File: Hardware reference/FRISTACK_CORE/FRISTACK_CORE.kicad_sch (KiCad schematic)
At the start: 72 parts, among them J1 USB_C_Receptacle_USB2.0_16P, J3 Conn_01x04_Pin, J4 Conn_01x09_Socket, J5 Conn_01x12_Socket, J6 Conn_01x12_Socket, J7 Conn_01x04_Pin, J8 Conn_01x02_Pin, U1 AZ1117-3.3, U2 USBLC6-2SC6, U3 ESP32-S3-MINI-1U, U4 SN65HVD232, Y1 32.768 kHz

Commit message: Updated CORE schematic and PCB design
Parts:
- removed J5, J6: Conn_01x12_Socket, Connector_PinSocket_2.54mm:PinSocket_1x12_P2.54mm_Vertical, symbol Connector:Conn_01x12_Socket
- added J5, J6: Conn_01x13_Socket, Connector_PinSocket_2.54mm:PinSocket_1x13_P2.54mm_Vertical, symbol Connector:Conn_01x13_Socket
- added J8: Conn_01x02_Pin, Connector_PinHeader_2.54mm:PinHeader_1x02_P2.54mm_Vertical, symbol Connector:Conn_01x02_Pin
- added R22: 120, Resistor_SMD:R_0603_1608Metric, symbol Device:R
- renumbered J8 to J2, R15 to R10, R16 to R11, R8 to R12, R9 to R13, R10 to R14, R11 to R15, R12 to R16, R13 to R17, R17 to R18, R18 to R19, R19 to R20, R20 to R21, R21 to R8, R14 to R9
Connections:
- net GPIO10 is gone; now on net CS: U3.14 (IO10)
- net GPIO11 is gone; now on net MISO: U3.15 (IO11)
- net GPIO12 is gone; now on net SCK: U3.16 (IO12)
- net +3V3: now also J5.13 (Pin_13)
- net +5V: now also J6.13 (Pin_13)
- net ADC_1: now also J5.2 (Pin_2)
- net CAN_D: now also U3.37 (IO41); no longer U3.18 (IO14)
- net CAN_H: now also J6.3 (Pin_3), R22.1
- net CAN_L: now also J6.2 (Pin_2), J8.2 (Pin_2)
- net CAN_R: now also U3.38 (IO42); no longer U3.17 (IO13)
- net CS: now also J6.7 (Pin_7); no longer U3.29 (IO34)
- net EN: now also J6.12 (Pin_12)
- net GND: now also J5.1 (Pin_1), J6.1 (Pin_1)
- net GPIO39: now also J6.8 (Pin_8)
- net I2S_DIN: now also J5.9 (Pin_9)
- net I2S_DOUT: now also J5.8 (Pin_8)
- net I2S_LRCK: now also J5.10 (Pin_10)
- net MISO: now also J6.6 (Pin_6); no longer U3.33 (IO37)
- net MOSI: now also U3.17 (IO13), J6.4 (Pin_4); no longer U3.31 (IO35)
- net SCK: now also J6.5 (Pin_5); no longer U3.32 (IO36)
- net SCL: now also J5.6 (Pin_6)
- net SDA: now also J5.7 (Pin_7)
- net UART0_RX: now also J6.10 (Pin_10)
- net UART0_TX: now also J6.11 (Pin_11)
- net USB_DN: now also U2.6 (I/O1); no longer U2.4 (I/O2)
- net USB_DN_2: now also U2.1 (I/O1), J5.11 (Pin_11); no longer U2.3 (I/O2)
- net USB_DP: now also U2.4 (I/O2); no longer U2.6 (I/O1)
- net USB_DP_2: now also U2.3 (I/O2), J5.12 (Pin_12); no longer U2.1 (I/O1)
- net GPIO17: now reaches U3.21 (IO17)
- net GPIO17: now also J5.4 (Pin_4)
- net GPIO18: now reaches U3.22 (IO18)
- net GPIO18: now also J5.3 (Pin_3)
- net GPIO40: now reaches U3.36 (IO40)
- net GPIO40: now also J6.9 (Pin_9)
- net GPIO38: no longer names the net of U3.34 (IO38)
- new net: J8.1 (Pin_1), R22.2
- new net GPIO14: J5.5 (Pin_5), U3.18 (IO14)
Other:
- note removed: "JST"
- moved on the sheet: C17, C18, C6, C7, C8, C9, D4, J7, R18, R19, S1, S2

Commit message: Added SENSOR-NODE and reworked CORE
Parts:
- removed C13: 22uF, Capacitor_SMD:C_0603_1608Metric, symbol Device:C
- removed C31: 2.2uF, Capacitor_SMD:C_0603_1608Metric, symbol Device:C
- removed C32: 100nF, Capacitor_SMD:C_0603_1608Metric, symbol Device:C
- removed C33: 1nF, Capacitor_SMD:C_0603_1608Metric, symbol Device:C
- removed D3: 1N5819WS, Diode_SMD:D_SOD-323, symbol Diode:1N5819WS
- removed J2: Conn_01x02_Pin, Connector_JST:JST_PH_S2B-PH-K_1x02_P2.00mm_Horizontal, symbol Connector:Conn_01x02_Pin
- removed J4: Conn_01x09_Socket, Connector_PinSocket_2.54mm:PinSocket_1x09_P2.54mm_Vertical, symbol Connector:Conn_01x09_Socket
- added D4: 1N5819WS, Diode_SMD:D_SOD-323, symbol Diode:1N5819WS
- added J3: Conn_01x02_Pin, Connector_PinHeader_2.54mm:PinHeader_1x02_P2.54mm_Vertical, symbol Connector:Conn_01x02_Pin
- added PROG1: Conn_01x04_Pin, Connector_JST:JST_PH_S4B-PH-K_1x04_P2.00mm_Horizontal, symbol Connector:Conn_01x04_Pin
- added R17: 10K, Resistor_SMD:R_0603_1608Metric, symbol Device:R
- added U4: FUSB42, Package_SO:VSSOP-10_3x3mm_P0.5mm, symbol Interface_USB:TS3USB30EDGSR
- R10: renamed from R12; value 2K2 -> 4K7
- R11: renamed from R13; value 2K2 -> 4K7
- R16: renamed from R10; value 0 -> 22
- R7: value 499 -> 22
- R8, R9: value 0 -> 22
- renumbered S2 to Boot1, C6 to C2, C7 to C3, C8 to C4, C9 to C5, C2 to C6, C3 to C7, C4 to C8, C5 to C9, D4 to D5, J5 to J4, J6 to J5, J8 to J6, R14 to R12, R15 to R13, R16 to R14, R17 to R15, R11 to R18, R22 to R19, R18 to R20, R19 to R21, R20 to R22, R21 to R23, S1 to RST1, J7 to TWAI1, U4 to U5, J3 to UART1
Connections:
- net +3V3: now also UART1.4 (Pin_4), PROG1.1 (Pin_1), R17.1, U4.10 (VCC); no longer UART1.3 (Pin_3)
- net ADC_1: now also J4.5 (Pin_5); no longer J4.2 (Pin_2)
- net GND: now also UART1.3 (Pin_3), PROG1.2 (Pin_2), U4.5 (GND), U4.9 (~{OE}); no longer UART1.4 (Pin_4)
- net GPIO14: now also J4.4 (Pin_4); no longer J4.5 (Pin_5)
- net GPIO17: now also J4.3 (Pin_3); no longer J4.4 (Pin_4)
- net GPIO18: now also J4.2 (Pin_2); no longer J4.3 (Pin_3)
- net DC: no longer names the net of U3.30 (IO48)
- net RST_LCD renamed GPIO47
- net GPIO47: now also D4.2 (A)
- net USB_DN renamed USB_N
- removed net USB_DN_2: J4.11 (Pin_11), R9.2, U2.1 (I/O1)
- net USB_DP renamed USB_P
- removed net USB_DP_2: J4.12 (Pin_12), R16.2, U2.3 (I/O2)
- new net: D4.1 (K), J3.2 (Pin_2), U4.1 (S)
- new net: J3.1 (Pin_1), R17.2
- new net USB_N_2: U2.1 (I/O1), U4.7 (D2-)
- new net USB_N_ESP: R9.2, U4.6 (D-)
- new net USB_N_HD: J4.12 (Pin_12), PROG1.3 (Pin_3), U4.2 (D1+)
- new net USB_P_2: U2.3 (I/O2), U4.3 (D2+)
- new net USB_P_ESP: R16.2, U4.4 (D+)
- new net USB_P_HD: J4.11 (Pin_11), PROG1.4 (Pin_4), U4.8 (D1-)
- no-connect marks 15 -> 16
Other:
- note removed: "Setup for ILI9341"
- moved on the sheet: C15, C16, R10, R11, R12, R13, R14, R15, R18, UART1, Y1

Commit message: Power management changes on CORE and SENSOR_NODE
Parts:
- removed Boot1, RST1: TL3315NF100Q, User_imports:SW_TL3315NF100Q, symbol User_imports:TL3315NF100Q
- removed C8: 0.1uF, Capacitor_SMD:C_0603_1608Metric, symbol Device:C
- removed C9: 10uF, Capacitor_SMD:C_0603_1608Metric, symbol Device:C
- removed D2: LED RED, LED_SMD:LED_0805_2012Metric, symbol Device:LED
- removed D4: 1N5819WS, Diode_SMD:D_SOD-323, symbol Diode:1N5819WS
- removed J3: Conn_01x02_Pin, Connector_PinHeader_2.54mm:PinHeader_1x02_P2.54mm_Vertical, symbol Connector:Conn_01x02_Pin
- removed R17: 10K, Resistor_SMD:R_0603_1608Metric, symbol Device:R
- removed U1: AZ1117-3.3, Package_TO_SOT_SMD:SOT-223, symbol Regulator_Linear:AZ1117-3.3
- removed U4: FUSB42, Package_SO:VSSOP-10_3x3mm_P0.5mm, symbol Interface_USB:TS3USB30EDGSR
- added L1: 2.2uH, Inductor_SMD:L_0805_2012Metric, symbol Device:L
- added S1, S2: TS-1088-AR02016, User_imports:SW_TS-1088-AR02016, symbol TS-1088-AR02016:TS-1088-AR02016
- added U1: TPS62840DLCR, User_imports:SON50P200X150X100-8N, symbol TPS62840DLCR:TPS62840DLCR
- C6: value 10uF -> 4.7uF
- C7: value 0.1uF -> 10uF
- R3: value 75 -> 267k
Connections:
- net USB_N_ESP is gone; now on net USB_N_2: R9.2
- net USB_N_HD is gone; now on net USB_N_2: J4.12 (Pin_12), PROG1.3 (Pin_3)
- net USB_P_ESP is gone; now on net USB_P_2: R16.2
- net USB_P_HD is gone; now on net USB_P_2: J4.11 (Pin_11), PROG1.4 (Pin_4)
- net +3V3: now also C7.1, L1.2, U1.8 (VOS); no longer R3.1
- net +5V: now also U1.2 (VIN), U1.4 (EN); no longer C7.1
- net EN: now also S1.2; no longer J5.12 (Pin_12)
- net GND: now also J5.8 (Pin_8), R3.2, S1.1, S2.1, U1.1 (GND), U1.3 (MODE), U1.6 (STOP)
- net GPIO0: now also S2.2
- net UART0_RX: now also J5.11 (Pin_11); no longer J5.10 (Pin_10)
- net UART0_TX: now also J5.12 (Pin_12); no longer J5.11 (Pin_11)
- net GPIO39 renamed RST
- net RST: now also J5.9 (Pin_9); no longer J5.8 (Pin_8)
- net GPIO40 renamed BOOT
- net BOOT: now also J5.10 (Pin_10); no longer J5.9 (Pin_9)
- net GPIO47: no longer names the net of U3.27 (IO47)
- new net: R3.1, U1.5 (VSET)
- new net: L1.1, U1.7 (SW)
- no-connect marks 16 -> 17
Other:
- moved on the sheet: C2, C3, C4, C5

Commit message: Added logos, annotations
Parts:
- added D2: 1N5819WS, Diode_SMD:D_SOD-323, symbol Diode:1N5819WS
- added J2: JTAG_PIN_HEADER, Connector_PinHeader_2.54mm:PinHeader_1x02_P2.54mm_Vertical, symbol Connector:Conn_01x02_Pin
- added J3: BAT, Connector_JST:JST_PH_S2B-PH-K_1x02_P2.00mm_Horizontal, symbol Connector:Conn_01x02_Pin
- C6, C7: footprint Capacitor_SMD:C_0603_1608Metric -> Capacitor_SMD:C_0402_1005Metric
- L1: footprint Inductor_SMD:L_0805_2012Metric -> User imports:INDC2016X120N
- R18: value ? -> 1M
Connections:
- net +3V3: now also TWAI1.4 (Pin_4); no longer TWAI1.3 (Pin_3)
- net +5V: now also D2.2 (A)
- net CAN_D: now also J2.2 (Pin_2)
- net CAN_R: now also J2.1 (Pin_1)
- net GND: now also TWAI1.3 (Pin_3), J3.2 (Pin_2); no longer TWAI1.4 (Pin_4)
- new net: D2.1 (K), J3.1 (Pin_1)

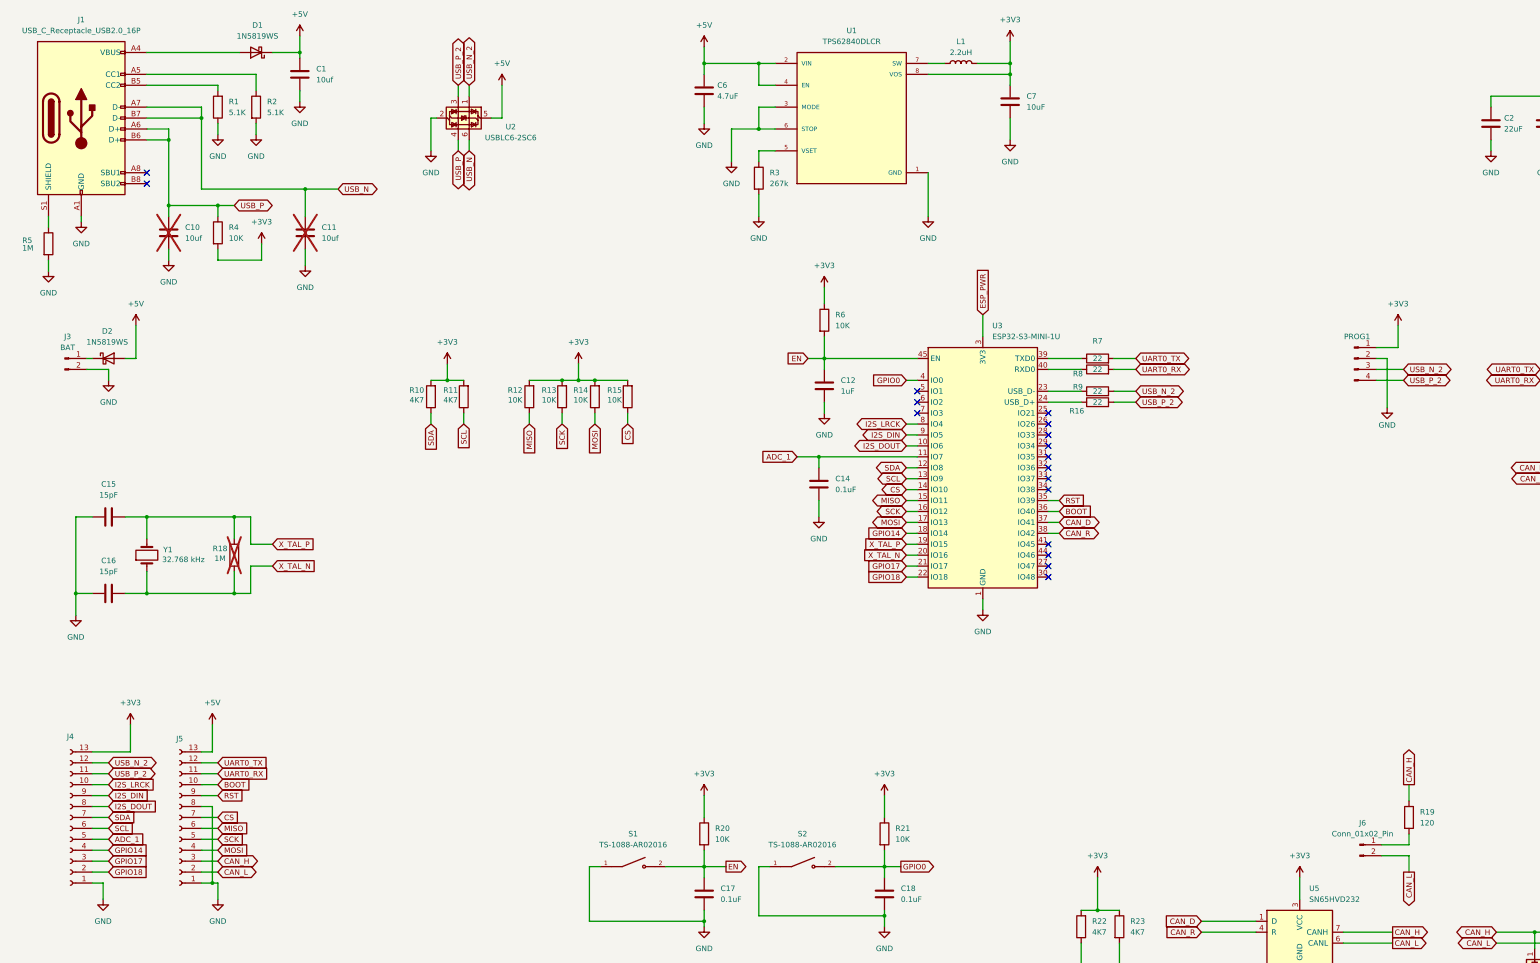
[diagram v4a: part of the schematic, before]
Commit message: Added USBSwitch to Core and added first version of Compatibility
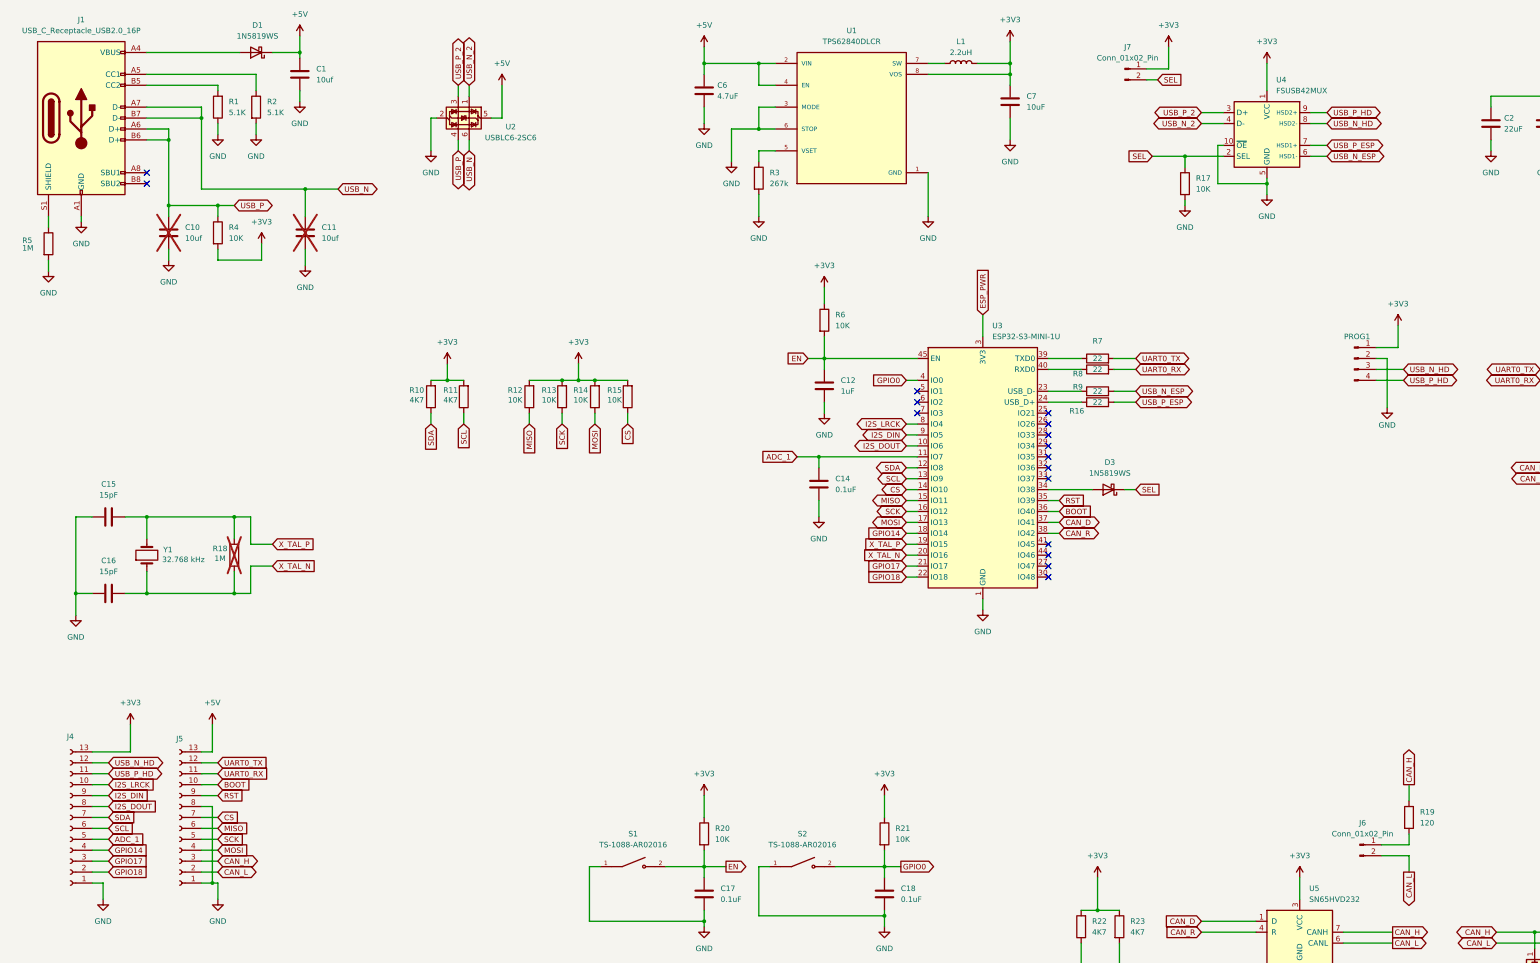
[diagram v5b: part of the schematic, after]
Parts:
- removed D2: 1N5819WS, Diode_SMD:D_SOD-323, symbol Diode:1N5819WS
- removed J3: BAT, Connector_JST:JST_PH_S2B-PH-K_1x02_P2.00mm_Horizontal, symbol Connector:Conn_01x02_Pin
- added D3: 1N5819WS, Diode_SMD:D_SOD-323, symbol Diode:1N5819WS
- added J7: Conn_01x02_Pin, Connector_PinHeader_2.54mm:PinHeader_1x02_P2.54mm_Vertical, symbol Connector:Conn_01x02_Pin
- added R17: 10K, Resistor_SMD:R_0603_1608Metric, symbol Device:R
- added U4: FSUSB42MUX, Package_SO:MSOP-10_3x3mm_P0.5mm, symbol Interface_USB:FSUSB42MUX
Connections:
- net +3V3: now also J7.1 (Pin_1), U4.1 (VCC)
- net GND: now also R17.2, U4.10 (~{OE}), U4.5 (GND)
- net USB_N_2: now also U4.4 (D-); no longer J4.12 (Pin_12), PROG1.3 (Pin_3), R9.2
- net USB_P_2: now also U4.3 (D+); no longer J4.11 (Pin_11), PROG1.4 (Pin_4), R16.2
- net at U3.34 (IO38): now also D3.2 (A)
- new net SEL: D3.1 (K), J7.2 (Pin_2), R17.1, U4.2 (SEL)
- new net USB_N_ESP: R9.2, U4.6 (HSD1-)
- new net USB_N_HD: J4.12 (Pin_12), PROG1.3 (Pin_3), U4.8 (HSD2-)
- new net USB_P_ESP: R16.2, U4.7 (HSD1+)
- new net USB_P_HD: J4.11 (Pin_11), PROG1.4 (Pin_4), U4.9 (HSD2+)
- no-connect marks 17 -> 16

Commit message: Reworked CORE and adjusted header pins
Added USB switch and MCP73871 for charging battery and powering the system. Changed GPIO14 to BAT, dedicated for battery.
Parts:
- added C15: 10uf, Capacitor_SMD:C_0402_1005Metric, symbol Device:C
- added C21, C22: 4.7uF, Capacitor_SMD:C_0402_1005Metric, symbol Device:C
- added R12: 20k, Resistor_SMD:R_0402_1005Metric, symbol Device:R
- added R13: 330k, Resistor_SMD:R_0402_1005Metric, symbol Device:R
- added R14: 110k, Resistor_SMD:R_0402_1005Metric, symbol Device:R
- added R15: 2k, Resistor_SMD:R_0402_1005Metric, symbol Device:R
- added R16, R17, R18, R20, R22, R23: 10k, Resistor_SMD:R_0402_1005Metric, symbol Device:R
- added TH1: 10k, Resistor_SMD:R_0603_1608Metric, symbol Device:Thermistor_NTC
- added U2: MCP73871-2CC, Package_DFN_QFN:QFN-20-1EP_4x4mm_P0.5mm_EP2.5x2.5mm, symbol Battery_Management:MCP73871-2CC
- C1: renamed from C19; footprint Capacitor_SMD:C_0603_1608Metric -> Capacitor_SMD:C_0402_1005Metric
- C10: renamed from C11; footprint Capacitor_SMD:C_0603_1608Metric -> Capacitor_SMD:C_0402_1005Metric
- C11: renamed from C24; footprint Capacitor_SMD:C_0603_1608Metric -> Capacitor_SMD:C_0402_1005Metric
- C12: renamed from C25; footprint Capacitor_SMD:C_0603_1608Metric -> Capacitor_SMD:C_0402_1005Metric
- C13: renamed from C26; footprint Capacitor_SMD:C_0603_1608Metric -> Capacitor_SMD:C_0402_1005Metric
- C14: renamed from C27; footprint Capacitor_SMD:C_0603_1608Metric -> Capacitor_SMD:C_0402_1005Metric
- C16: renamed from C28; footprint Capacitor_SMD:C_0603_1608Metric -> Capacitor_SMD:C_0402_1005Metric
- C17: renamed from C29; footprint Capacitor_SMD:C_0603_1608Metric -> Capacitor_SMD:C_0402_1005Metric
- C19: renamed from C30; footprint Capacitor_SMD:C_0603_1608Metric -> Capacitor_SMD:C_0402_1005Metric
- C2: renamed from C20; footprint Capacitor_SMD:C_0603_1608Metric -> Capacitor_SMD:C_0402_1005Metric
- C20: renamed from C17; footprint Capacitor_SMD:C_0603_1608Metric -> Capacitor_SMD:C_0402_1005Metric
- C23: renamed from C18; footprint Capacitor_SMD:C_0603_1608Metric -> Capacitor_SMD:C_0402_1005Metric
- C24: renamed from C14; footprint Capacitor_SMD:C_0603_1608Metric -> Capacitor_SMD:C_0402_1005Metric
- C25: renamed from C12; footprint Capacitor_SMD:C_0603_1608Metric -> Capacitor_SMD:C_0402_1005Metric
- C27: renamed from C2; footprint Capacitor_SMD:C_0603_1608Metric -> Capacitor_SMD:C_0402_1005Metric
- C28: renamed from C3; footprint Capacitor_SMD:C_0603_1608Metric -> Capacitor_SMD:C_0402_1005Metric
- C29: renamed from C4; footprint Capacitor_SMD:C_0603_1608Metric -> Capacitor_SMD:C_0402_1005Metric
- C3: renamed from C15; footprint Capacitor_SMD:C_0603_1608Metric -> Capacitor_SMD:C_0402_1005Metric
- C30: renamed from C5; footprint Capacitor_SMD:C_0603_1608Metric -> Capacitor_SMD:C_0402_1005Metric
- C4: renamed from C16; footprint Capacitor_SMD:C_0603_1608Metric -> Capacitor_SMD:C_0402_1005Metric
- C5: renamed from C21; footprint Capacitor_SMD:C_0603_1608Metric -> Capacitor_SMD:C_0402_1005Metric
- C6: renamed from C10; footprint Capacitor_SMD:C_0603_1608Metric -> Capacitor_SMD:C_0402_1005Metric
- C7: renamed from C22; footprint Capacitor_SMD:C_0603_1608Metric -> Capacitor_SMD:C_0402_1005Metric
- C8: renamed from C23; footprint Capacitor_SMD:C_0603_1608Metric -> Capacitor_SMD:C_0402_1005Metric
- C9: renamed from C1; footprint Capacitor_SMD:C_0603_1608Metric -> Capacitor_SMD:C_0402_1005Metric
- L1: footprint User imports:INDC2016X120N -> User_imports:INDC2016X120N
- R1: renamed from R5; footprint Resistor_SMD:R_0603_1608Metric -> Resistor_SMD:R_0402_1005Metric
- R10: renamed from R2; footprint Resistor_SMD:R_0603_1608Metric -> Resistor_SMD:R_0402_1005Metric
- R11: renamed from R15; footprint Resistor_SMD:R_0603_1608Metric -> Resistor_SMD:R_0402_1005Metric
- R19: renamed from R20; footprint Resistor_SMD:R_0603_1608Metric -> Resistor_SMD:R_0402_1005Metric
- R2: renamed from R10; footprint Resistor_SMD:R_0603_1608Metric -> Resistor_SMD:R_0402_1005Metric
- R21: renamed from R3; footprint Resistor_SMD:R_0603_1608Metric -> Resistor_SMD:R_0402_1005Metric
- R24: renamed from R21; footprint Resistor_SMD:R_0603_1608Metric -> Resistor_SMD:R_0402_1005Metric
- R25: renamed from R6; footprint Resistor_SMD:R_0603_1608Metric -> Resistor_SMD:R_0402_1005Metric
- R26: renamed from R22; footprint Resistor_SMD:R_0603_1608Metric -> Resistor_SMD:R_0402_1005Metric
- R27: renamed from R23; footprint Resistor_SMD:R_0603_1608Metric -> Resistor_SMD:R_0402_1005Metric
- R29: renamed from R17; footprint Resistor_SMD:R_0603_1608Metric -> Resistor_SMD:R_0402_1005Metric
- R3: renamed from R11; footprint Resistor_SMD:R_0603_1608Metric -> Resistor_SMD:R_0402_1005Metric
- R30: renamed from R7; footprint Resistor_SMD:R_0603_1608Metric -> Resistor_SMD:R_0402_1005Metric
- R31: renamed from R8; footprint Resistor_SMD:R_0603_1608Metric -> Resistor_SMD:R_0402_1005Metric
- R32: renamed from R9; footprint Resistor_SMD:R_0603_1608Metric -> Resistor_SMD:R_0402_1005Metric
- R33: renamed from R16; footprint Resistor_SMD:R_0603_1608Metric -> Resistor_SMD:R_0402_1005Metric
- R34: renamed from R19; footprint Resistor_SMD:R_0603_1608Metric -> Resistor_SMD:R_0402_1005Metric
- R4: renamed from R12; footprint Resistor_SMD:R_0603_1608Metric -> Resistor_SMD:R_0402_1005Metric
- R5: renamed from R13; footprint Resistor_SMD:R_0603_1608Metric -> Resistor_SMD:R_0402_1005Metric
- R6: renamed from R1; footprint Resistor_SMD:R_0603_1608Metric -> Resistor_SMD:R_0402_1005Metric
- R7: renamed from R4; footprint Resistor_SMD:R_0603_1608Metric -> Resistor_SMD:R_0402_1005Metric
- R8: renamed from R14; footprint Resistor_SMD:R_0603_1608Metric -> Resistor_SMD:R_0402_1005Metric
- R9: renamed from R18; footprint Resistor_SMD:R_0603_1608Metric -> Resistor_SMD:R_0402_1005Metric
- renumbered C6 to C18, C7 to C26, D3 to D2, D5 to D3, J4 to J1, J1 to J2, J5 to J3, J7 to J4, J6 to J5, J2 to J6, U2 to U1, U1 to U3, U3 to U4, U4 to U5, U5 to U6
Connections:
- net +3V3: now also R20.1, R22.1, R23.1
- net GND: now also C15.2, C21.2, C22.2, R12.2, R14.2, R15.2, R16.2, R17.2, TH1.2, U2.10 (V_{SS}), U2.11 (V_{SS}), U2.21 (V_{SS}), U2.3 (SEL)
- net STAT2: now reaches U4.25 (IO21)
- net STAT2: now also R23.2, U2.7 (STAT2)
- net STAT1: now reaches U4.27 (IO47)
- net STAT1: now also R22.2, U2.8 (STAT1/~{LBO})
- net GPIO48: now reaches U4.30 (IO48)
- net GPIO48: now also R17.1, U2.9 (~{TE})
- net GPIO1: now reaches U4.5 (IO1)
- net GPIO1: now also R16.1, U2.4 (PROG2)
- net PG: now reaches U4.6 (IO2)
- net PG: now also R20.2, U2.6 (~{PG})
- net +5V renamed OUT/BAT
- net OUT/BAT: now also C22.1, U2.1 (OUT), U2.20 (OUT); no longer C9.1, D1.1 (K), U1.5 (VBUS)
- net GPIO14: no longer names the net of U4.18 (IO14)
- net GPIO14: no longer J1.4 (Pin_4)
- new net: R13.2, R14.1, U2.2 (VPCC)
- new net: TH1.1, U2.5 (THERM)
- new net: R18.2, U2.17 (CE)
- new net: R12.1, U2.12 (PROG3)
- new net: R15.1, U2.13 (PROG1)
- new net BAT: C21.1, J1.4 (Pin_4), U2.14 (V_{BAT}), U2.15 (V_{BAT}), U2.16 (V_{BAT_SENSE})
- new net VBUS: C15.1, C9.1, D1.1 (K), R13.1, R18.1, U1.5 (VBUS), U2.18 (IN), U2.19 (IN)
- no-connect marks 16 -> 12
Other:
- note added: "Nejaku ochrannu diodku na USB"
- moved on the sheet: C18, C24, C25, C26, D2, J4, J6, L1, PROG1, R11, R2, R21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

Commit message: Changed jumpers with DIP switches and adjusted copper areas
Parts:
- removed J4, J5: Conn_01x02_Pin, Connector_PinHeader_2.54mm:PinHeader_1x02_P2.54mm_Vertical, symbol Connector:Conn_01x02_Pin
- added SW1, SW2: SW_DIP_x01, Button_Switch_THT:SW_DIP_SPSTx01_Slide_6.7x4.1mm_W7.62mm_P2.54mm_LowProfile, symbol Switch:SW_DIP_x01
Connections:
- net +3V3: now also SW2.1
- net CAN_L: now also SW1.2
- net SEL: now also SW2.2
- net at R34.2: now also SW1.1
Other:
- note removed: "Nejaku ochrannu diodku na USB"
